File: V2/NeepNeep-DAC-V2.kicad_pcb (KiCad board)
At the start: 2 copper layers, 24 x 24 mm, 18 parts, among them J1 Conn_02x03_Odd_Even, Q1 MMBT3904, U2 W25Q32JVSS, U3 ATtiny85-20SU

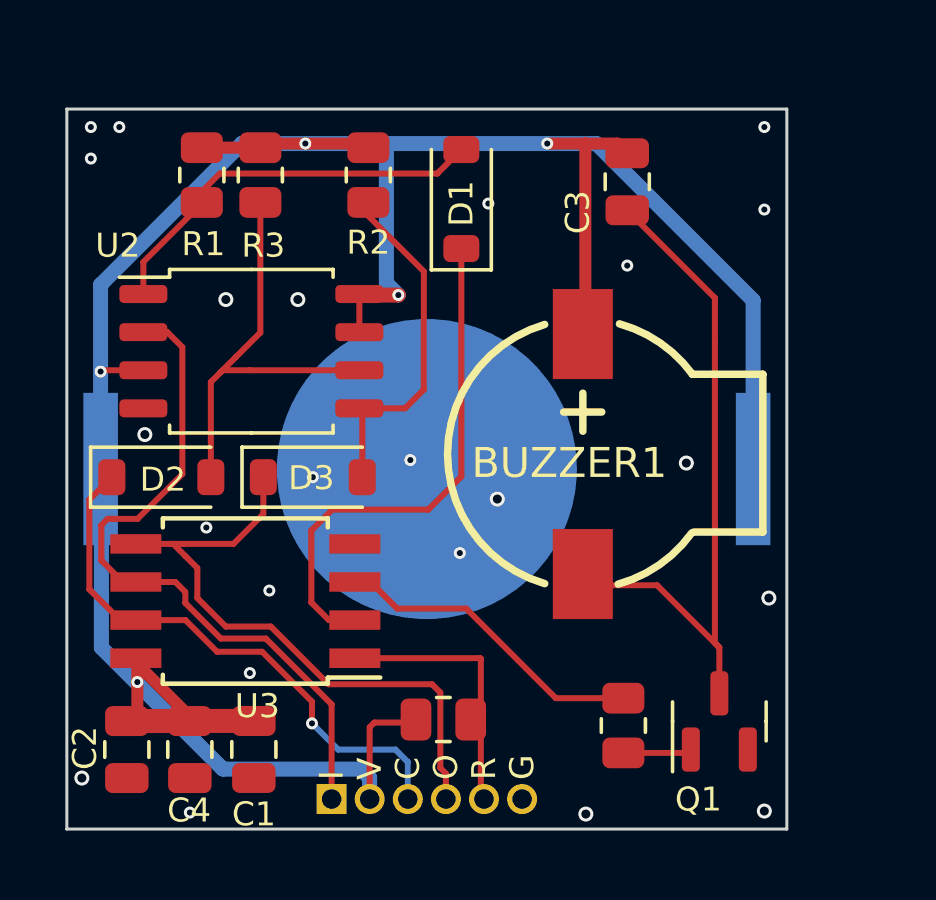
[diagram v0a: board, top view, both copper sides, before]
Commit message: Commit: A	V2/NeepNeep-DAC-V2-backups/NeepNeep-DAC-V2-2026-02-06_155723.zip A	V2/NeepNeep-DAC-V2-backups/NeepNeep-DAC-V2-2026-02-06_161052.zip A	V2/NeepNeep-DAC-V2-backups/NeepNeep-DAC-V2-2026-02-06_161649.zip A	V2/NeepNeep-DAC-V2-backups/NeepNeep-DAC-V2-2026-02-09_173407.zip M	V2/NeepNeep-DAC-V2.kicad_pcb M	V2/NeepNeep-DAC-V2.kicad_prl M	V2/NeepNeep-DAC-V2.kicad_sch A	V2/NeepNeep-DAC-V2.kicad_sch-bak A	V2/NeepNeep-DAC-V2.png
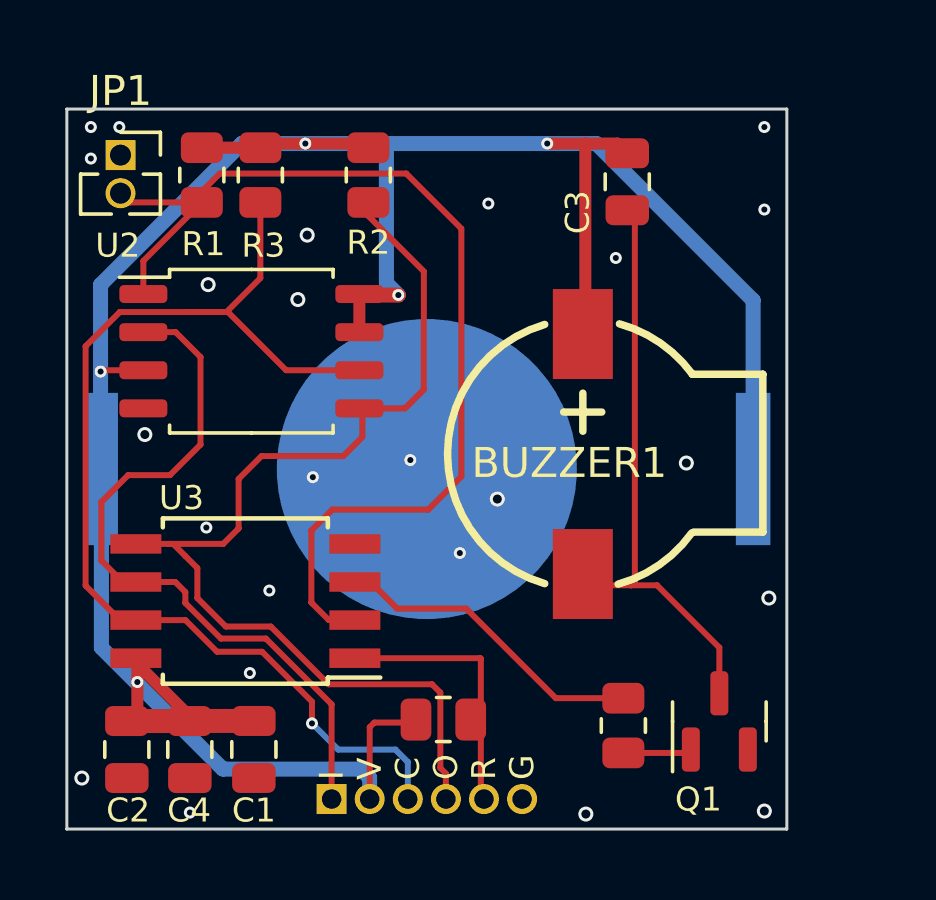
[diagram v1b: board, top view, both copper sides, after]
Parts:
- removed D1, D2, D3: 1N4148W, Diode_SMD:D_SOD-123
- added JP1: Jumper_2_Open, Connector_PinSocket_1.27mm:PinSocket_1x02_P1.27mm_Vertical, F.Cu at (89.8, 89.5)
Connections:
- R1 pad 2: Net-(D1-A) -> PB3
- R2 pad 2: Net-(D3-A) -> PB0/MOSI
- R3 pad 2: Net-(D2-A) -> PB2/SCK
- U2 pad 1: Net-(D1-A) -> PB3
- U2 pad 5: Net-(D3-A) -> PB0/MOSI
- U2 pad 6: Net-(D2-A) -> PB2/SCK
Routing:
- net PB2/SCK: track 18.7 -> 38.6 mm
- net PB3: track 17.4 -> 35.5 mm
- net PB0/MOSI: track 21.2 -> 35.7 mm
- net Net-(D2-A): track 14.5 -> 0.00 mm
- net Net-(D1-A): track 13.7 -> 0.00 mm
- net Net-(D3-A): track 11.7 -> 0.00 mm
- net Net-(BUZZER1--): track 23.0 -> 19.8 mm
- net PB1/MISO: track 23.4 -> 24.3 mm
- net GND: vias 23 -> 24
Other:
- board text added: "${TITLE} REV: ${REVISION}"
- board text added: "DATE: ${CURRENT_DATE}"
- board text removed: "20260116-1250"
- board text removed: "ATTINY85 DAC"
- board text removed: "NeepNeep"

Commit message: Commit: A	V2/NeepNeep-DAC-V2-backups/NeepNeep-DAC-V2-2026-02-09_174934.zip A	V2/NeepNeep-DAC-V2-backups/NeepNeep-DAC-V2-2026-02-10_125359.zip A	V2/NeepNeep-DAC-V2-backups/NeepNeep-DAC-V2-2026-02-10_130055.zip M	V2/NeepNeep-DAC-V2.kicad_pcb M	V2/NeepNeep-DAC-V2.kicad_prl M	V2/NeepNeep-DAC-V2.kicad_sch A	V2/Thumbs.db
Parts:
- added R4: 100k, Resistor_SMD:R_0805_2012Metric, F.Cu at (107.3, 108.6)
- Q1: value MMBT3904 -> BSS138
- moved R7 1.27 mm to (105.3, 108.6)
- moved Q1 0.24 mm to (110.0, 108.5)
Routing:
- net Net-(Q1-G): track 2.30 -> 3.79 mm
- net PB4: track 10.6 -> 9.30 mm

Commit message: Commit: A	V2/NeepNeep-DAC-V2-backups/NeepNeep-DAC-V2-2026-02-11_154859.zip A	V2/NeepNeep-DAC-V2-backups/NeepNeep-DAC-V2-2026-02-11_164151.zip A	V2/NeepNeep-DAC-V2-backups/NeepNeep-DAC-V2-2026-02-11_165528.zip M	V2/NeepNeep-DAC-V2.kicad_pcb M	V2/NeepNeep-DAC-V2.kicad_prl M	V2/NeepNeep-DAC-V2.kicad_sch
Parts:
- removed JP1: Jumper_2_Open, Connector_PinSocket_1.27mm:PinSocket_1x02_P1.27mm_Vertical
- added J2: Conn_01x03_Pin, Connector_PinHeader_1.27mm:PinHeader_1x03_P1.27mm_Vertical, F.Cu at (106.3, 110.8)
- moved C4 19.6 mm to (96.5, 90.2)
- moved C1 2.14 mm to (92.1, 109.5)
- moved Q1 1.32 mm to (110.2, 107.2)
- moved R7 1.25 mm to (105.5, 107.3)
- moved R4 1.24 mm to (107.4, 107.3)
- moved R2 0.40 mm to (98.5, 90.2)
- moved C2 0.11 mm to (90.0, 109.5)
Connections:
- J1 pad 5: PB5/RESET -> PB3
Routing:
- net 3.3v: track 92.5 -> 104.3 mm
- net PB5/RESET: track 8.93 -> 16.4 mm, vias 0 -> 2
- net PB3: track 35.5 -> 42.6 mm
- net Net-(BUZZER1--): track 19.8 -> 18.8 mm
- net GND: vias 24 -> 21

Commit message: Commit: M	README.md A	V2/NeepNeep-DAC-V2-backups/NeepNeep-DAC-V2-2026-02-12_124743.zip A	V2/NeepNeep-DAC-V2-backups/NeepNeep-DAC-V2-2026-02-12_132550.zip A	V2/NeepNeep-DAC-V2-backups/NeepNeep-DAC-V2-2026-02-12_133556.zip A	V2/NeepNeep-DAC-V2-backups/NeepNeep-DAC-V2-2026-02-12_142149.zip A	V2/NeepNeep-DAC-V2-backups/NeepNeep-DAC-V2-2026-02-12_143905.zip A	V2/NeepNeep-DAC-V2-backups/NeepNeep-DAC-V2-2026-02-12_170144.zip M	V2/NeepNeep-DAC-V2.kicad_pcb M	V2/NeepNeep-DAC-V2.kicad_prl M	V2/NeepNeep-DAC-V2.kicad_pro M	V2/NeepNeep-DAC-V2.kicad_sch A	V2/bom/NeepNeep-DAC-V2-ibom.html M	V2/fp-info-cache A	V2/ibom.config.ini A	V2/jlcpcb/gerber/NeepNeep-DAC-V2-CuBottom.gbr A	V2/jlcpcb/gerber/NeepNeep-DAC-V2-CuTop.gbr A	V2/jlcpcb/gerber/NeepNeep-DAC-V2-EdgeCuts.gbr A	V2/jlcpcb/gerber/NeepNeep-DAC-V2-MaskBottom.gbr A	V2/jlcpcb/gerber/NeepNeep-DAC-V2-MaskTop.gbr A	V2/jlcpcb/gerber/NeepNeep-DAC-V2-NPTH-drl_map.pdf A	V2/jlcpcb/gerber/NeepNeep-DAC-V2-NPTH.drl A	V2/jlcpcb/gerber/NeepNeep-DAC-V2-PTH-drl_map.pdf A	V2/jlcpcb/gerber/NeepNeep-DAC-V2-PTH.drl A	V2/jlcpcb/gerber/NeepNeep-DAC-V2-PasteBottom.gbr A	V2/jlcpcb/gerber/NeepNeep-DAC-V2-PasteTop.gbr A	V2/jlcpcb/gerber/NeepNeep-DAC-V2-SilkBottom.gbr A	V2/jlcpcb/gerber/NeepNeep-DAC-V2-SilkTop.gbr A	V2/jlcpcb/gerber/NeepNeep-DAC-V2-VScore.gbr A	V2/jlcpcb/production_files/BOM-NeepNeep-DAC-V2.csv A	V2/jlcpcb/production_files/CPL-NeepNeep-DAC-V2.csv A	V2/jlcpcb/production_files/GERBER-NeepNeep-DAC-V2.zip A	V2/jlcpcb/project.db
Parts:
- J1: footprint Global Kicad FootprintLibrary:PRG-Header_1x06_P1.27mm -> Niffum-Connector:SPI-Header_1x06_P1.27mm
- J2: footprint Connector_PinHeader_1.27mm:PinHeader_1x03_P1.27mm_Vertical -> Niffum-Connector:UPDI PinHeader_1x03_P1.27mm_Vertical
- moved J2 16.4 mm to (89.9, 111.0)
- moved R6 6.99 mm to (93.6, 107.6), turned to -90 degrees
- moved C4 6.41 mm to (90.0, 90.3)
- moved R2 6.25 mm to (92.2, 90.3)
- moved U1 2.70 mm to (94.4, 101.7)
- moved C3 2.56 mm to (109.0, 89.3), turned to 0 degrees
- moved R3 2.20 mm to (96.6, 90.3)
- moved C1 2.09 mm to (91.2, 107.6)
- moved C2 2.04 mm to (89.2, 107.6)
- moved R1 1.99 mm to (94.5, 90.3)
- moved Q1 0.80 mm to (110.2, 108.0)
- moved R4 0.60 mm to (107.4, 108.0)
- moved R7 0.60 mm to (105.5, 108.0)
- moved U2 0.20 mm to (94.2, 95.9), turned to 180 degrees
- moved J1 0.08 mm to (96.9, 111.0)
- renumbered U3 to U1
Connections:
- J1 pad 1: PB1/MISO -> 3.3v
- J1 pad 2: 3.3v -> GND
- J1 pad 3: PB2/SCK -> PB3
- J1 pad 4: PB0/MOSI -> PB1/MISO
- J1 pad 5: PB3 -> PB0/MOSI
- J1 pad 6: GND -> PB2/SCK
- J2 pad 1: 3.3v -> GND
- J2 pad 3: GND -> 3.3v
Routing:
- net 3.3v: track 104.3 -> 92.9 mm, vias 5 -> 7
- net PB3: track 42.6 -> 32.7 mm
- net Net-(BUZZER1--): track 18.8 -> 25.1 mm
- net PB0/MOSI: track 35.8 -> 31.7 mm, vias 0 -> 2
- net PB4: track 8.96 -> 12.6 mm
- net PB5/RESET: track 16.4 -> 13.1 mm, vias 2 -> 0
- net PB2/SCK: track 38.3 -> 36.5 mm, vias 1 -> 3
- net PB1/MISO: track 24.0 -> 25.4 mm, vias 0 -> 2
- net GND: track 0.00 -> 0.07 mm, vias 21 -> 26
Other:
- board text added: "${TITLE} REV: ${REVISION} DATE: ${CURRENT_DATE}"
- board text added: "SPI"
- board text added: "UPDI"
- board text removed: "${TITLE} REV: ${REVISION}"
- board text removed: "DATE: ${CURRENT_DATE}"

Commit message: Commit: D	V2/NeepNeep-DAC-V2-backups/NeepNeep-DAC-V2-2026-02-12_132550.zip A	V2/NeepNeep-DAC-V2-backups/NeepNeep-DAC-V2-2026-02-13_132614.zip A	V2/NeepNeep-DAC-V2-backups/NeepNeep-DAC-V2-2026-02-13_133905.zip A	V2/NeepNeep-DAC-V2-backups/NeepNeep-DAC-V2-2026-02-13_135245.zip A	V2/NeepNeep-DAC-V2-backups/NeepNeep-DAC-V2-2026-02-13_140056.zip A	V2/NeepNeep-DAC-V2-backups/NeepNeep-DAC-V2-2026-02-13_141120.zip M	V2/NeepNeep-DAC-V2.kicad_pcb M	V2/NeepNeep-DAC-V2.kicad_sch
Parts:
- U1: value ATtiny85-20SU -> ATtiny412-SS; footprint Package_SO:SOIC-8W_5.3x5.3mm_P1.27mm -> Package_SO:SOIC-8_3.9x4.9mm_P1.27mm
- moved U1 0.79 mm to (93.6, 101.7), turned to 0 degrees
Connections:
- net PB2/SCK renamed FLASH_CLK
- net PB3 renamed FLASH_CS
- net PB4 renamed SPEAKER
- J1 pad 4: PB1/MISO -> FLASH_DO
- J1 pad 5: PB0/MOSI -> FLASH_DI
- J2 pad 2: PB5/RESET -> RESET
- R2 pad 2: PB0/MOSI -> FLASH_DI
- R6 pad 2: PB5/RESET -> RESET
- U1 pad 1: PB5/RESET -> 3.3v
- U1 pad 4: GND -> FLASH_DI
- U1 pad 5: PB0/MOSI -> FLASH_DO
- U1 pad 6: PB1/MISO -> RESET
- U1 pad 8: 3.3v -> GND
- U2 pad 2: PB1/MISO -> FLASH_DO
- U2 pad 5: PB0/MOSI -> FLASH_DI
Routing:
- net FLASH_CS: track 32.7 -> 0.04 mm
- net PB0/MOSI: track 31.7 -> 0.00 mm, vias 2 -> 0
- net FLASH_DI: track 0.00 -> 29.3 mm
- net PB1/MISO: track 25.4 -> 0.00 mm, vias 2 -> 0
- net FLASH_CLK: track 36.5 -> 14.2 mm, vias 3 -> 1
- net PB5/RESET: track 13.1 -> 0.00 mm
- net SPEAKER: track 12.6 -> 0.03 mm
- net FLASH_DO: track 0.00 -> 11.1 mm
- net 3.3v: track 92.9 -> 83.2 mm, vias 7 -> 6
- net RESET: track 0.00 -> 5.45 mm
- net GND: vias 26 -> 21

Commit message: Commit: D	V2/NeepNeep-DAC-V2-backups/NeepNeep-DAC-V2-2026-02-13_132614.zip D	V2/NeepNeep-DAC-V2-backups/NeepNeep-DAC-V2-2026-02-13_133905.zip D	V2/NeepNeep-DAC-V2-backups/NeepNeep-DAC-V2-2026-02-13_135245.zip D	V2/NeepNeep-DAC-V2-backups/NeepNeep-DAC-V2-2026-02-13_140056.zip A	V2/NeepNeep-DAC-V2-backups/NeepNeep-DAC-V2-2026-02-13_141833.zip A	V2/NeepNeep-DAC-V2-backups/NeepNeep-DAC-V2-2026-02-13_162142.zip R055	V2/NeepNeep-DAC-V2-backups/NeepNeep-DAC-V2-2026-02-13_141120.zip	V2/NeepNeep-DAC-V2-backups/NeepNeep-DAC-V2-2026-02-13_163143.zip A	V2/NeepNeep-DAC-V2-backups/NeepNeep-DAC-V2-2026-02-13_163758.zip A	V2/NeepNeep-DAC-V2-backups/NeepNeep-DAC-V2-2026-02-13_165231.zip A	V2/NeepNeep-DAC-V2-backups/NeepNeep-DAC-V2-2026-02-13_171821.zip M	V2/NeepNeep-DAC-V2.kicad_pcb M	V2/NeepNeep-DAC-V2.kicad_pro
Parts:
- moved R3 6.45 mm to (90.2, 90.3)
- moved C4 4.31 mm to (94.3, 90.3)
- moved R1 2.41 mm to (96.9, 90.3)
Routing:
- net FLASH_CS: track 0.04 -> 38.8 mm, vias 0 -> 3
- net SPEAKER: track 0.03 -> 20.8 mm, vias 0 -> 2
- net FLASH_CLK: track 14.2 -> 31.9 mm, vias 1 -> 2
- net 3.3v: track 83.2 -> 97.0 mm, vias 6 -> 8
- net FLASH_DO: track 11.1 -> 24.8 mm
- net RESET: track 5.45 -> 13.5 mm, vias 0 -> 2
- net FLASH_DI: track 29.3 -> 32.3 mm, vias 0 -> 1
- net GND: vias 21 -> 22
